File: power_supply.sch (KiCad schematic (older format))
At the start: 71 parts, among them IC1 TPS54561DPRT, Q1 BSS138APW, Q2 BSS138-7-F, U1 AP62301WU-7, U2 AP62301WU-7, U3 AP62301WU-7, U4 74LVC1G123GN

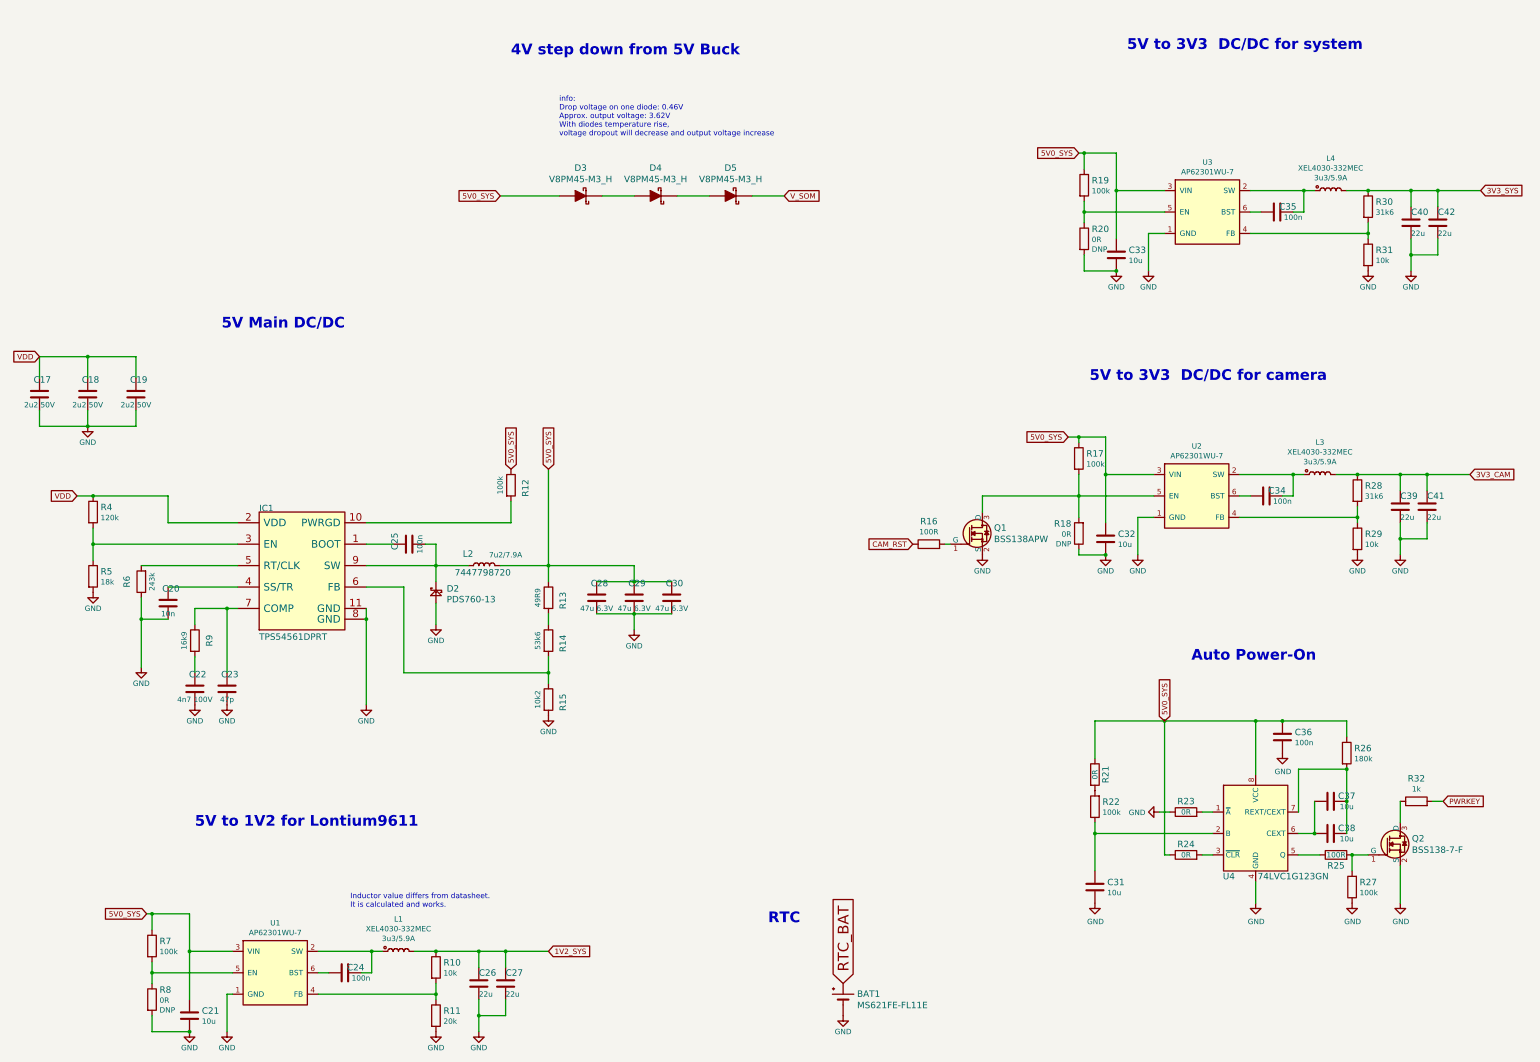
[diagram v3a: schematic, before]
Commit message: Routed CAM, LCD, USB Debug differential pairs with tuning
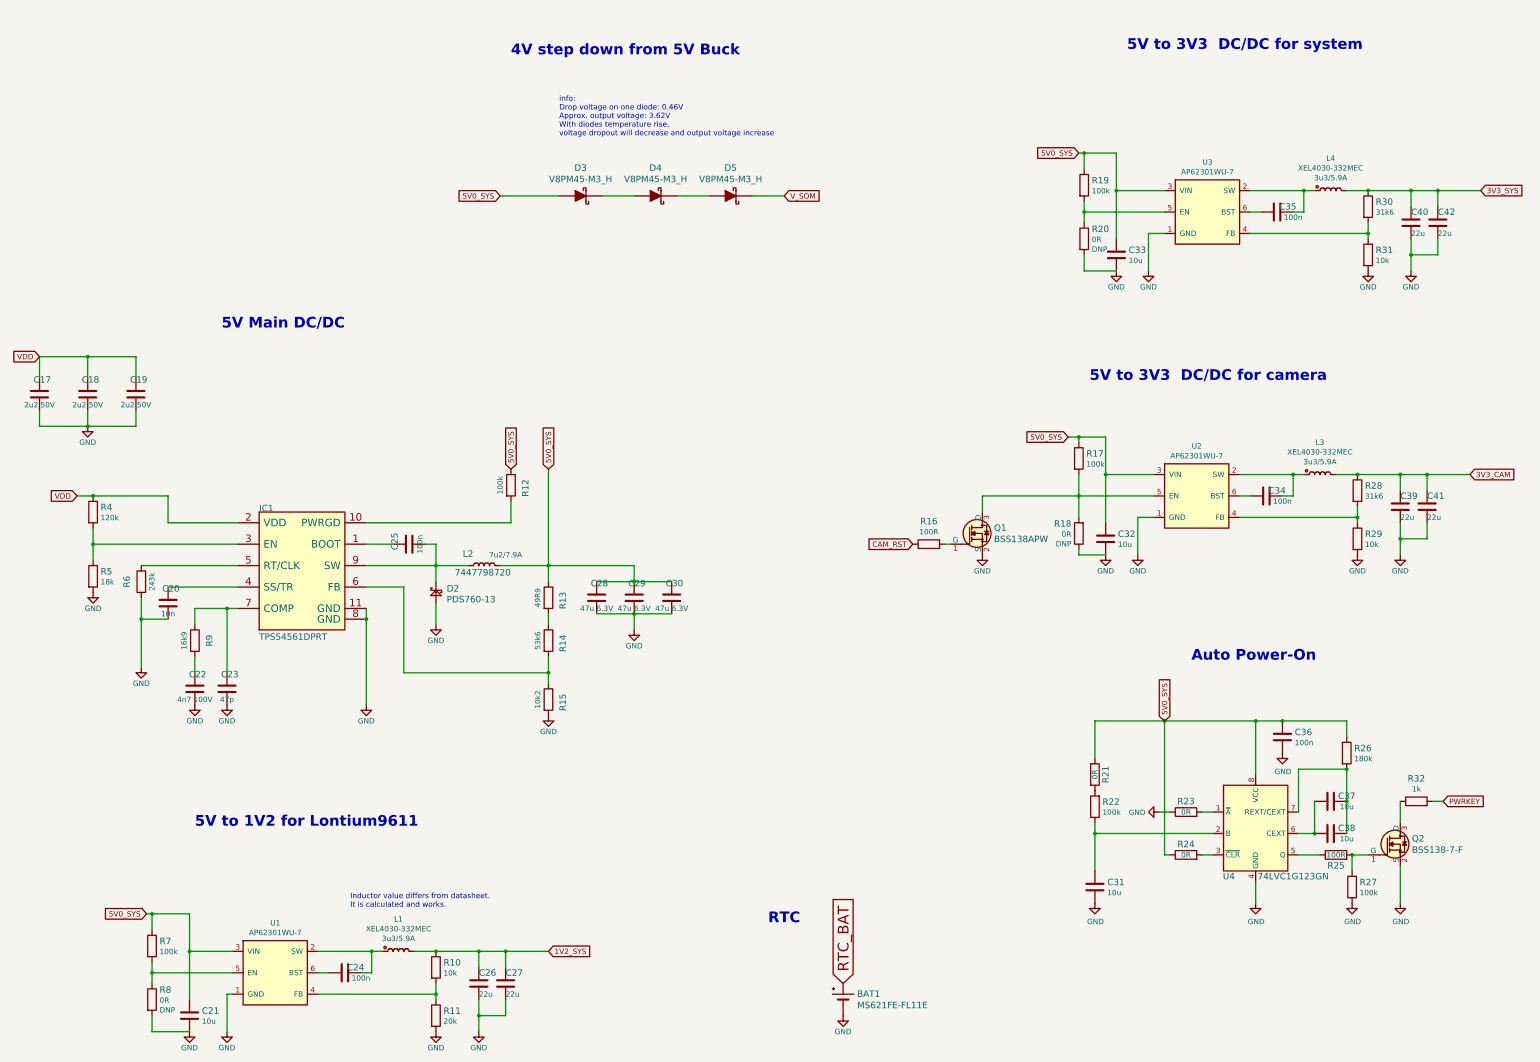
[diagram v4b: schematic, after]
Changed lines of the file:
@@
 Wire Wire Line
 	4750 5850 4450 5850
-$Comp
-L sc606-baseboard:GND #PWR033
-U 1 1 6241B50A
-P 4450 6400
-F 0 "#PWR033" H 4450 6150 50  0001 C CNN
-F 1 "GND" H 4450 6250 50  0000 C CNN
-F 2 "" H 4450 6400 50  0001 C CNN
-F 3 "" H 4450 6400 50  0001 C CNN
-	1    4450 6400
-	1    0    0    -1
-$EndComp
 Wire Wire Line
 	4450 6400 4450 6200
@@
 Wire Wire Line
 	10500 3100 10800 3100
-Connection ~ 10800 3100
 $Comp
 L sc606-baseboard:R_100k_0402 R19
@@
 Wire Wire Line
 	10450 5750 10700 5750
-Connection ~ 10700 5750
 Wire Wire Line
 	10450 5200 10450 5000
@@
 Wire Wire Line
 	1800 10200 2150 10200
-Connection ~ 2150 10200
 Wire Wire Line
 	1800 9250 1800 9100
@@
 Text GLabel 750  3900 0    50   Input ~ 0
 VDD
+$Comp
+L sc606-baseboard:GND #PWR033
+U 1 1 6241B50A
+P 4450 6400
+F 0 "#PWR033" H 4450 6150 50  0001 C CNN
+F 1 "GND" H 4450 6250 50  0000 C CNN
+F 2 "" H 4450 6400 50  0001 C CNN
+F 3 "" H 4450 6400 50  0001 C CNN
+	1    4450 6400
+	1    0    0    -1
+$EndComp
 $EndSCHEMATC

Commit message: Cleaned and added testpoints to spoer supply sch
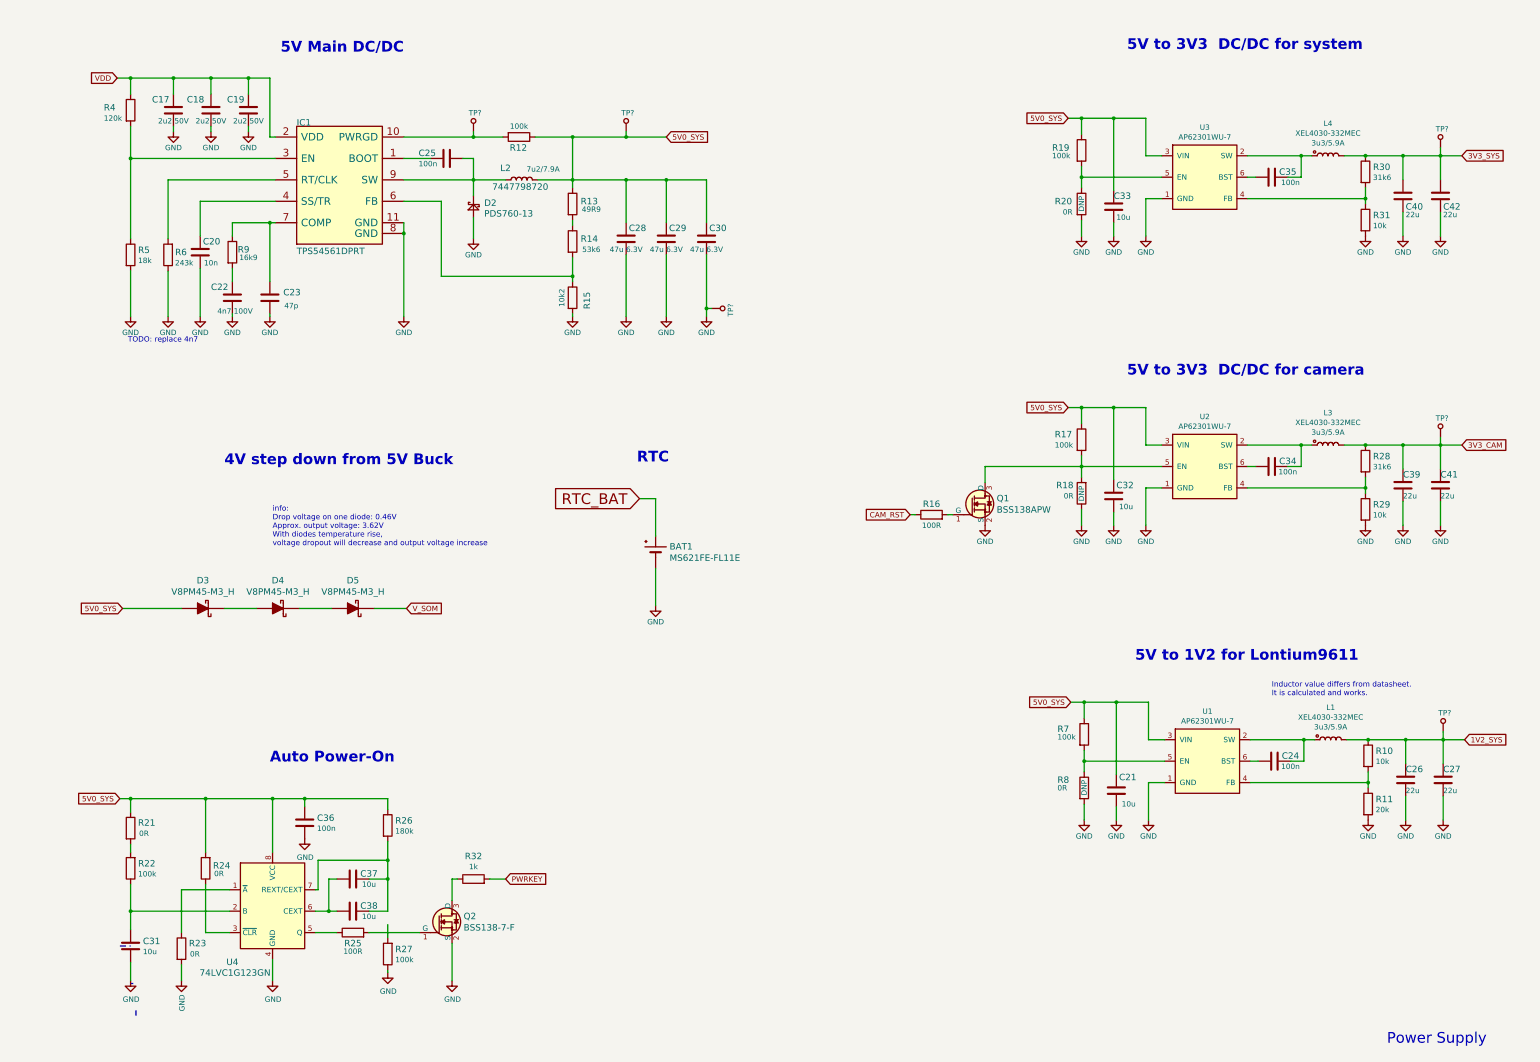
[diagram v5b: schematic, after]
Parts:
- added TP? (x6): TP_SMD_0_75MM, sc606-baseboard-footprints:Testpoint_smd_0_75mm, symbol sc606-baseboard:TP_SMD_0_75MM
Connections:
- net 1V2_SYS: now also TP?.1
- net 3V3_CAM: now also TP?.1
- net 3V3_SYS: now also TP?.1
- net 5V0_SYS: now also R24.2, TP?.1; no longer R24.1
- net GND: now also R23.2, TP?.1; no longer R23.1
- net at IC1.10 (PWRGD), R12.2: now also TP?.1
- net at Q2.1 (G), R25.2: no longer R27.2
- net at U4.1 (~A): now also R23.1; no longer R23.2
- net at U4.3 (~CLR): now also R24.1; no longer R24.2
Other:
- note added: "Power Supply"
- note added: "TODO: replace 4n7"
- moved on the sheet: BAT1, C17, C18, C19, C20, C21, C22, C23, C24, C25, C26, C27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

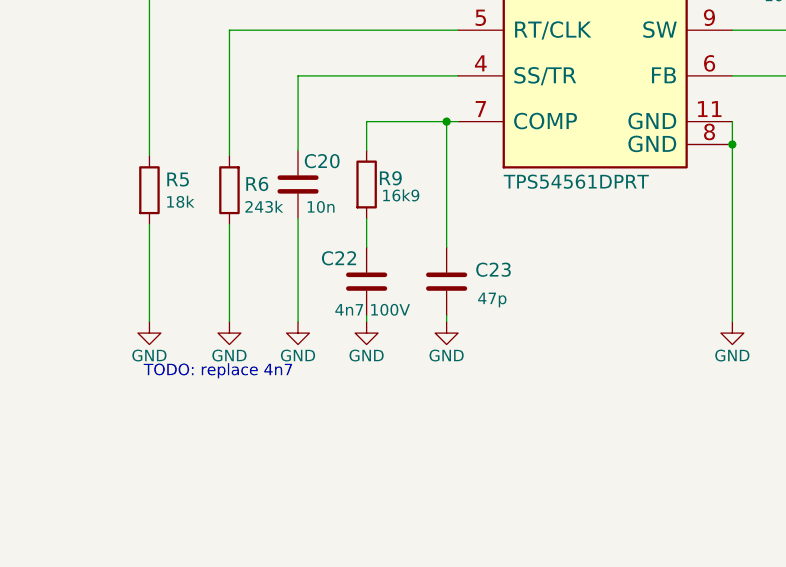
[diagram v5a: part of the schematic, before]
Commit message: Solved DRC problems with HDMI and CSI
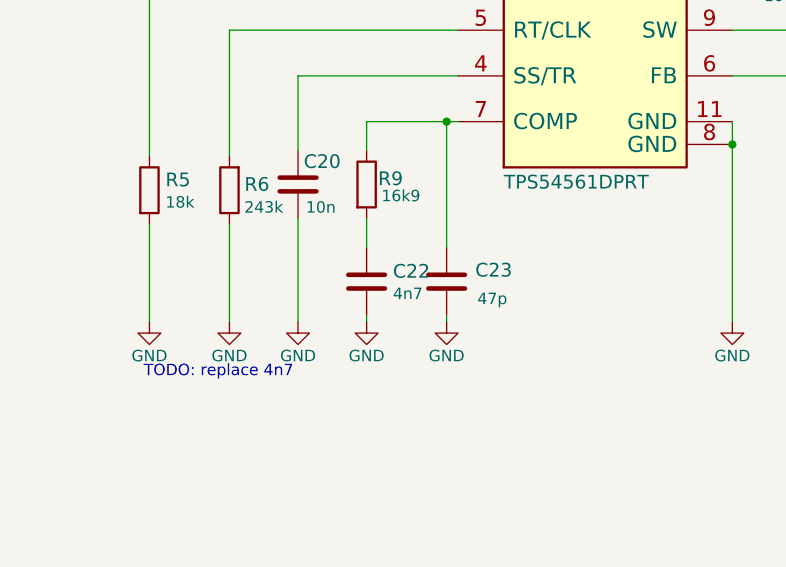
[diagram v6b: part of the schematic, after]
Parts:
- C22: value C_4n7_0805 -> C_4n7_0402; Val 4n7 100V -> 4n7
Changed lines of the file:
@@
-$EndComp
-$Comp
-L sc606-baseboard:C_4n7_0402 C22
-U 1 1 62404528
-P 2550 3350
-F 0 "C22" H 2350 3450 60  0000 L CNN
-F 1 "C_4n7_0805" H 2550 3200 60  0001 C CNN
-F 2 "sc606-baseboard-footprints:0402-cap" H 2750 3550 60  0001 L CNN
-F 3 "" H 2550 3350 50  0001 C CNN
-F 4 "TDK" H 2750 3750 60  0001 L CNN "Manufacturer"
-F 5 "CGA2B3X7S2A472K050BB" H 2750 3650 60  0001 L CNN "MPN"
-F 6 "4n7 100V" H 2575 3225 50  0000 C CNN "Val"
-	1    2550 3350
-	1    0    0    -1
 $EndComp
 $Comp
@@
 Wire Wire Line
 	13850 7400 13850 7475
+$Comp
+L sc606-baseboard:C_4n7_0402 C22
+U 1 1 621128AC
+P 2550 3350
+F 0 "C22" H 2665 3395 60  0000 L CNN
+F 1 "C_4n7_0402" H 2550 3200 60  0001 C CNN
+F 2 "sc606-baseboard-footprints:0402-cap" H 2750 3550 60  0001 L CNN
+F 3 "" H 2550 3350 50  0001 C CNN
+F 4 "TDK" H 2750 3750 60  0001 L CNN "Manufacturer"
+F 5 "CGA2B3X7S2A472K050BB" H 2750 3650 60  0001 L CNN "MPN"
+F 6 "4n7" H 2665 3297 50  0000 L CNN "Val"
+	1    2550 3350
+	1    0    0    -1
+$EndComp
 $EndSCHEMATC
